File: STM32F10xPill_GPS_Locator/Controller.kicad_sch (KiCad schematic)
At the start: 9 parts, among them U1 STM32F100C4Tx, Y1 16MHz, Y2 32.768kHz

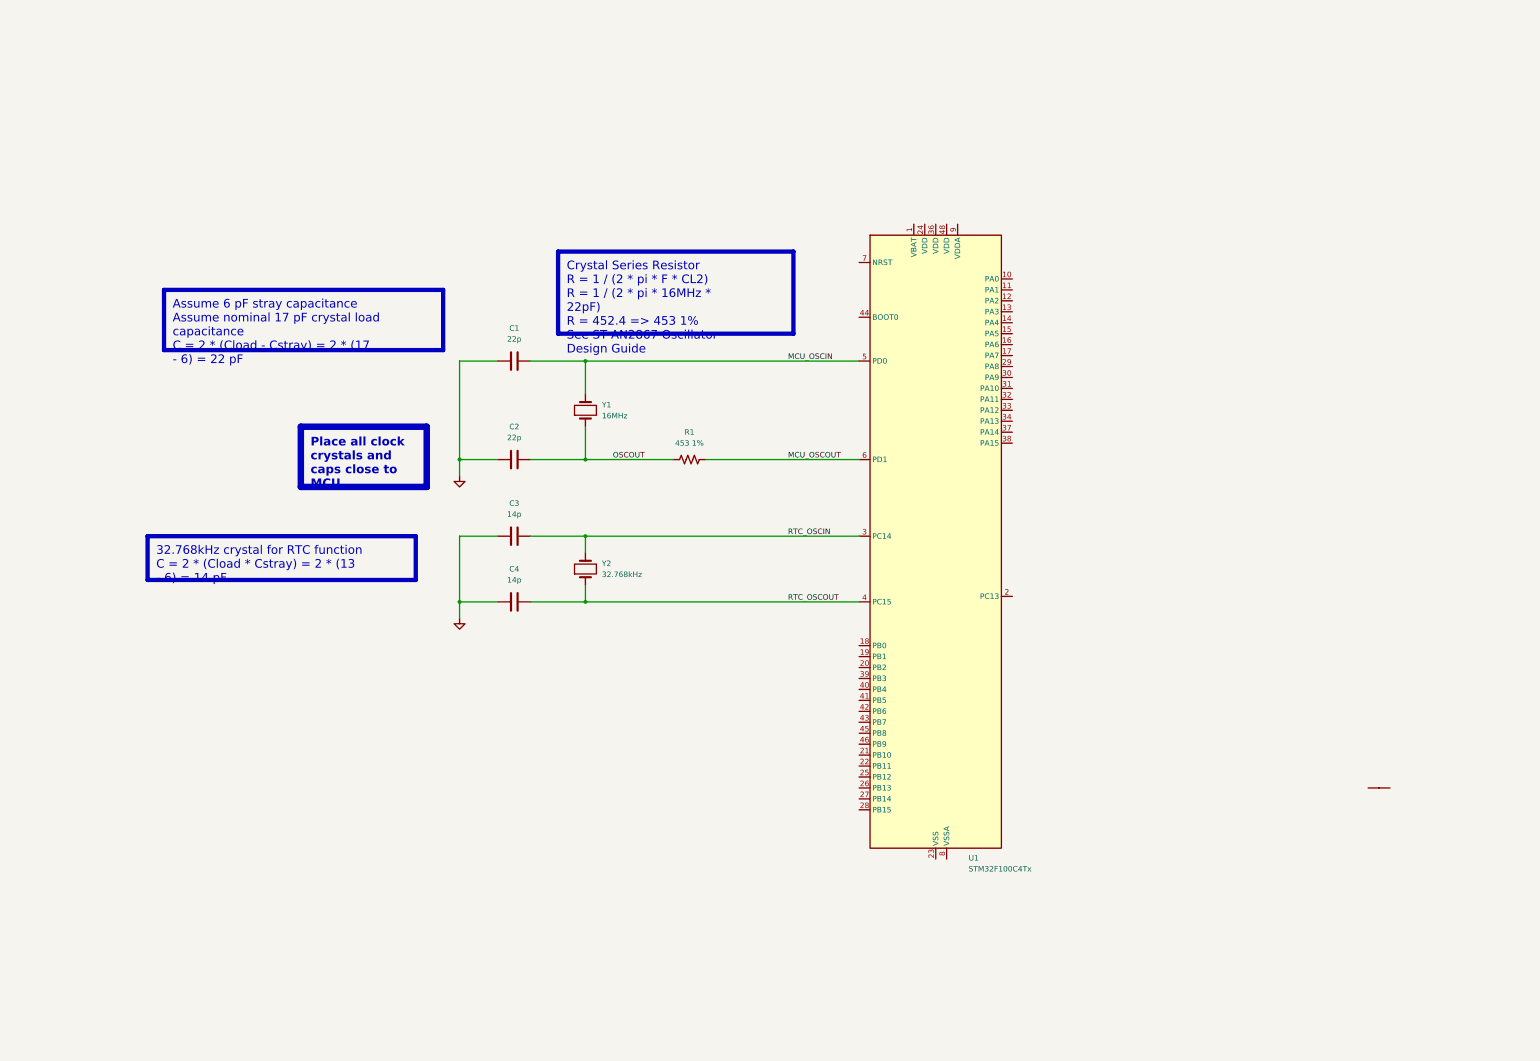
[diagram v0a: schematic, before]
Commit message: Add schematic reset, boot, SWD, and some peripherals
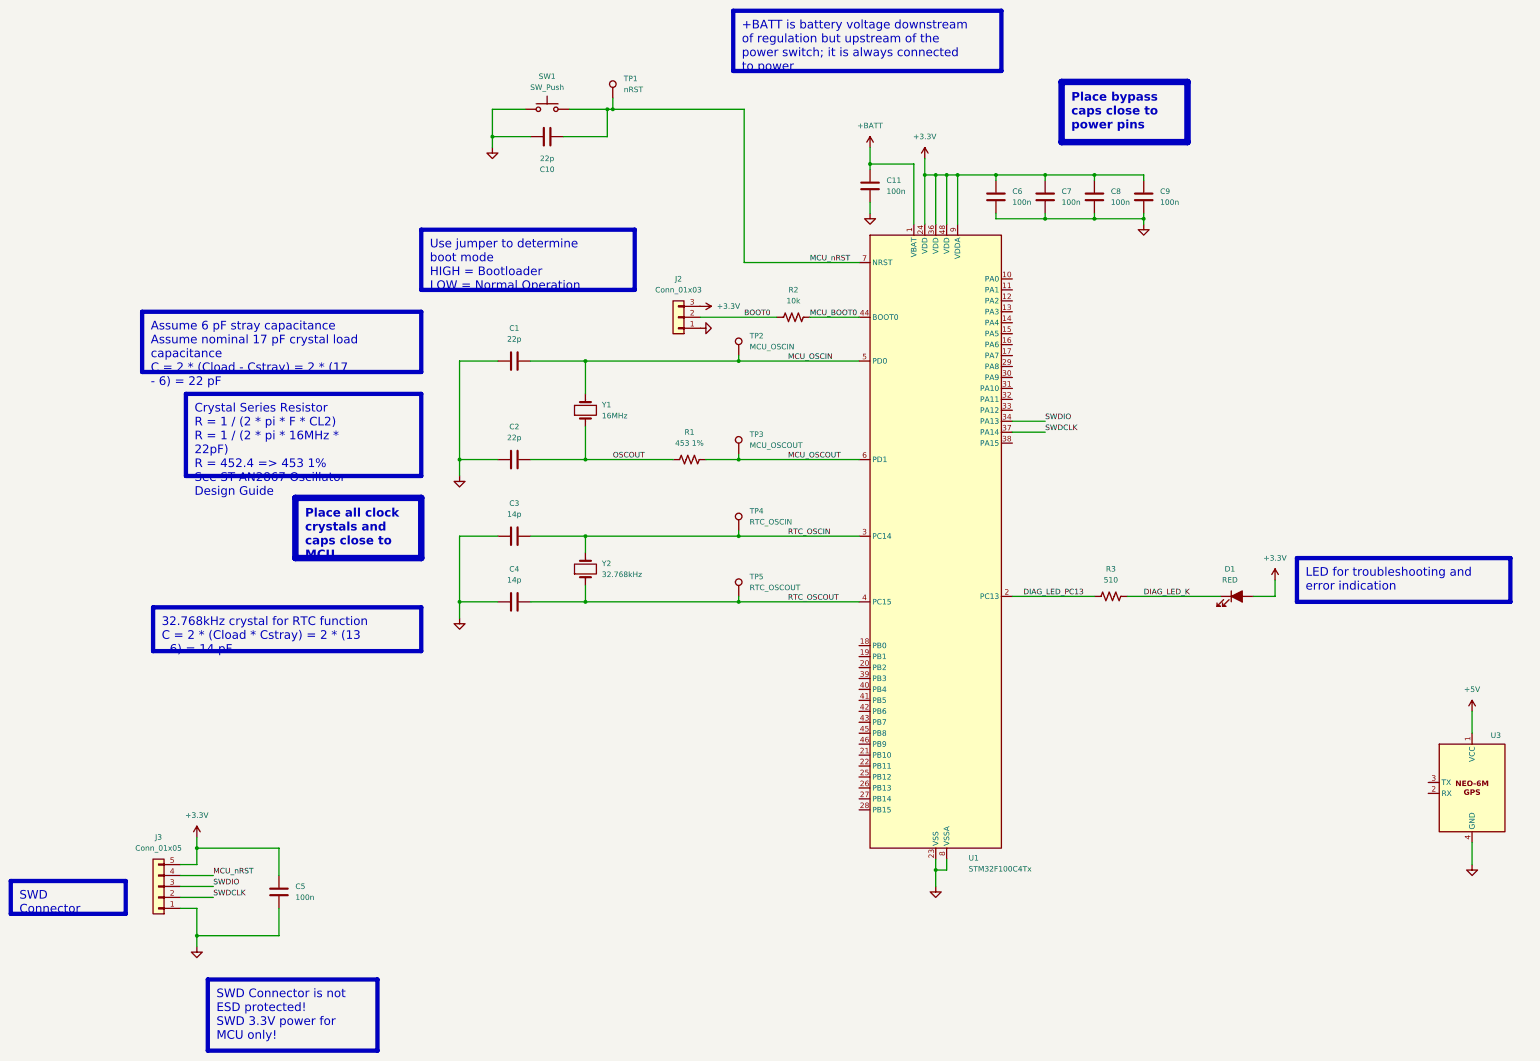
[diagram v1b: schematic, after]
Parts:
- removed U2: ~, symbol Utilities:Net_Tie
- added C10: 22p, symbol Device:C
- added C11, C5, C6, C7, C8, C9: 100n, symbol Device:C
- added D1: RED, symbol Device:LED_Filled
- added J2: Conn_01x03, symbol Connector_Generic:Conn_01x03
- added J3: Conn_01x05, symbol Connector_Generic:Conn_01x05
- added R2: 10k, symbol Device:R_US
- added R3: 510, symbol Device:R_US
- added SW1: SW_Push, symbol Switch:SW_Push
- added TP1: nRST, symbol Connector:TestPoint
- added TP2: MCU_OSCIN, symbol Connector:TestPoint
- added TP3: MCU_OSCOUT, symbol Connector:TestPoint
- added TP4: RTC_OSCIN, symbol Connector:TestPoint
- added TP5: RTC_OSCOUT, symbol Connector:TestPoint
- added U3: ~, symbol Modules:NEO-6M_Daughter_Board
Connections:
- net GND: now also U1.23 (VSS), U1.35 (VSS), U1.47 (VSS), U1.8 (VSSA), C10.1, C11.1, C5.1, C6.1, C7.1, C8.1, C9.1, J2.1 (Pin_1), J3.1 (Pin_1), SW1.1, U3.4 (GND)
- net MCU_OSCIN: now also TP2.1
- net MCU_OSCOUT: now also TP3.1
- net RTC_OSCIN: now also TP4.1
- net RTC_OSCOUT: now also TP5.1
- net +BATT: now reaches U1.1 (VBAT)
- net +BATT: now also C11.2
- net DIAG_LED_PC13: now reaches U1.2 (PC13)
- net DIAG_LED_PC13: now also R3.2
- net +3.3V: now reaches U1.24 (VDD)
- net +3.3V: now also U1.36 (VDD), U1.48 (VDD), U1.9 (VDDA), C5.2, C6.2, C7.2, C8.2, C9.2, D1.2 (A), J2.3 (Pin_3), J3.5 (Pin_5)
- net SWDIO: now reaches U1.34 (PA13)
- net SWDIO: now also J3.3 (Pin_3)
- net SWDCLK: now reaches U1.37 (PA14)
- net SWDCLK: now also J3.2 (Pin_2)
- net MCU_BOOT0: now reaches U1.44 (BOOT0)
- net MCU_BOOT0: now also R2.2
- net MCU_nRST: now reaches U1.7 (NRST)
- net MCU_nRST: now also C10.2, J3.4 (Pin_4), SW1.2, TP1.1
- new net +5V: U3.1 (VCC)
- new net BOOT0: J2.2 (Pin_2), R2.1
- new net DIAG_LED_K: D1.1 (K), R3.1
